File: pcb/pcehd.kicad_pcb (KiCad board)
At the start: 2 copper layers, 158 parts, among them J1 HDMI_CONN, P1 JTAG_CONN, Q1 BC847, Q2 BC847, U1 AP7361, U10 SN74LVCC4245APW, U11 SN74LVCC4245APW, U12 10CL025YE144C8N, U13 IS25LP016D-JBLE, U14 SN74LVCC4245APW, U15 TLV70012, U16 TLV70025, U17 TLV70012, U18 SN74LVCC4245APW, U19 SN74LVC3G17, U2 ADV7513, U3 TLV70018, U4 PCEngineExpansion, U5 FS7140-01G-XTD, U6 PCM1808PWR, U7 SI5351C-B, U8 74153, U9 SN74LVCC4245APW, Y1 25.000MHz

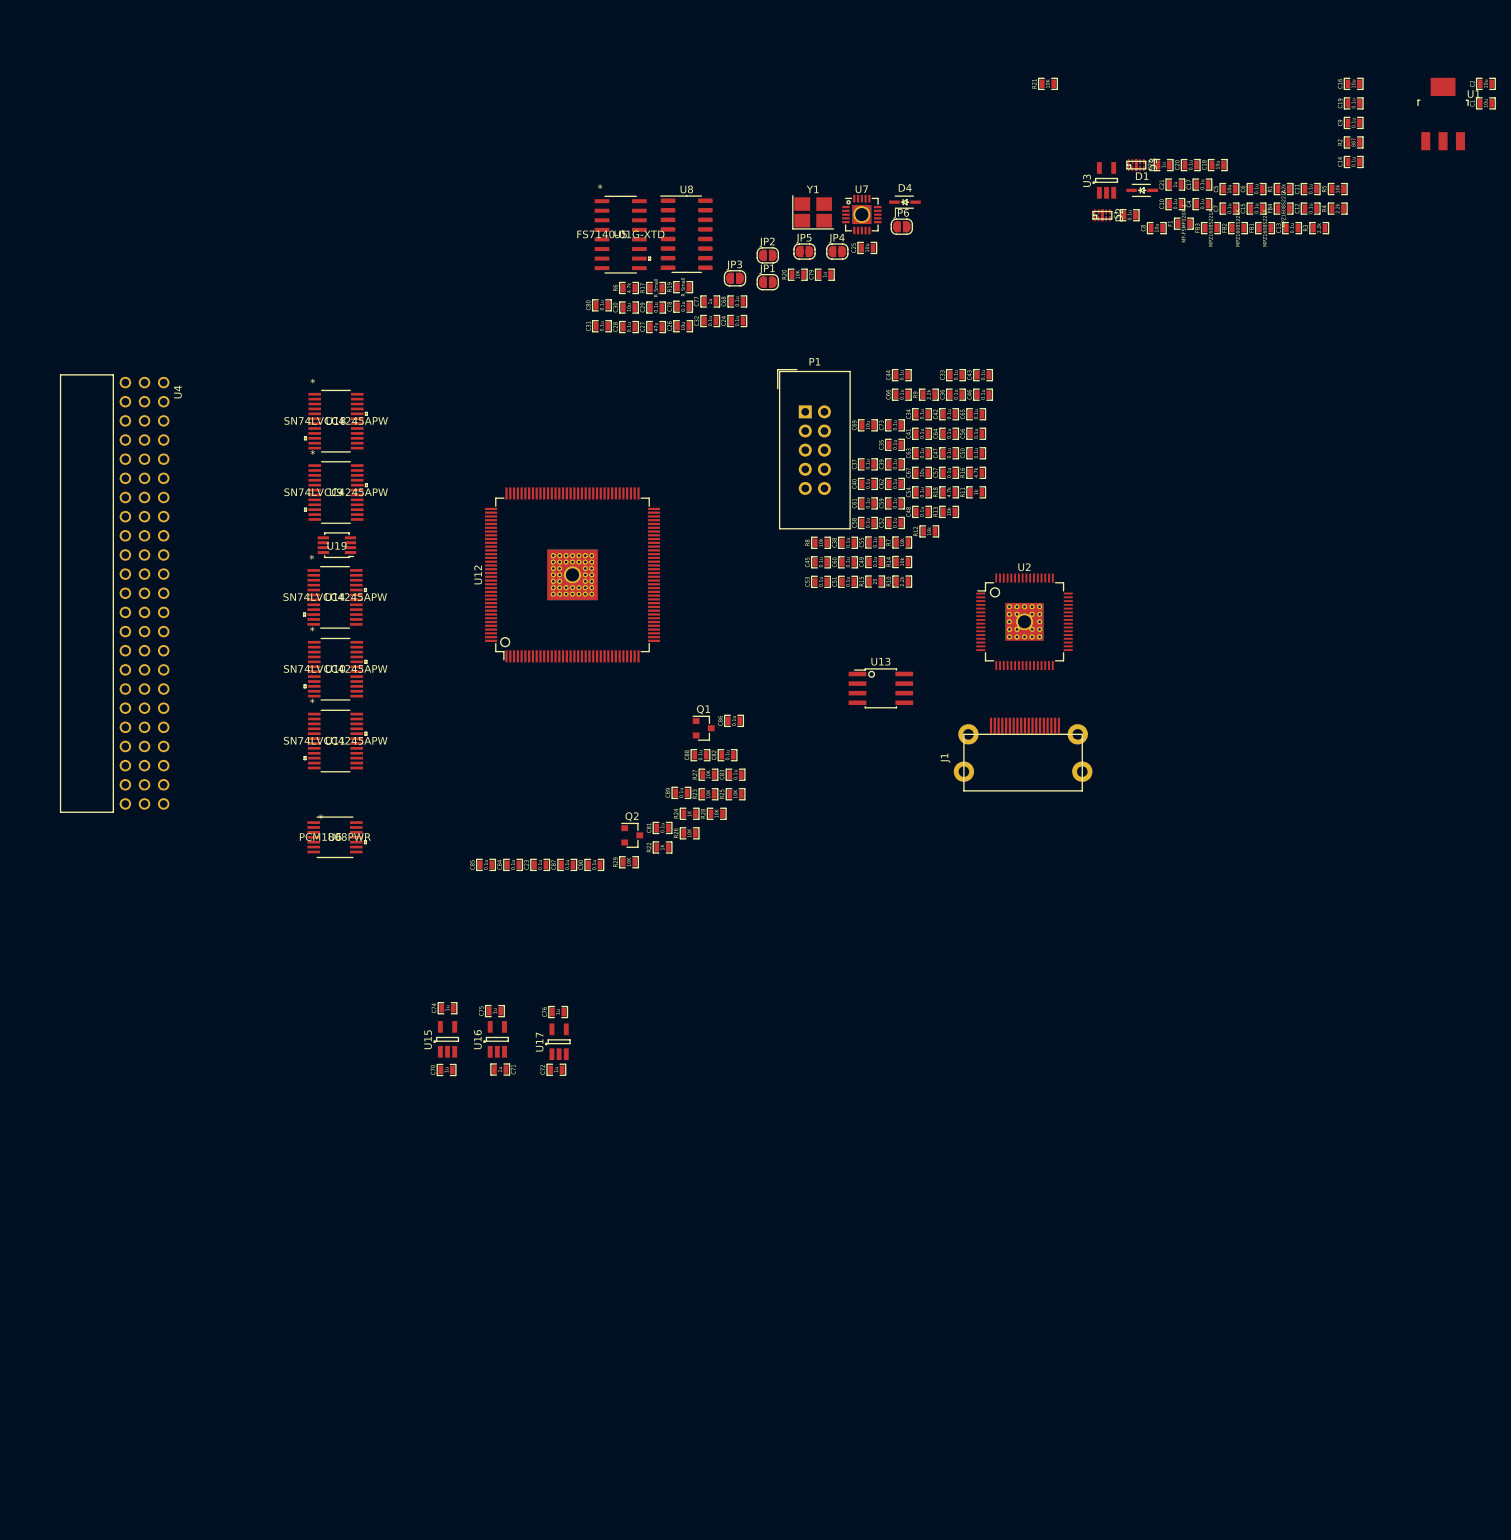
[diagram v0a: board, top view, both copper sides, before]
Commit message: Expansion connection re-order for layout
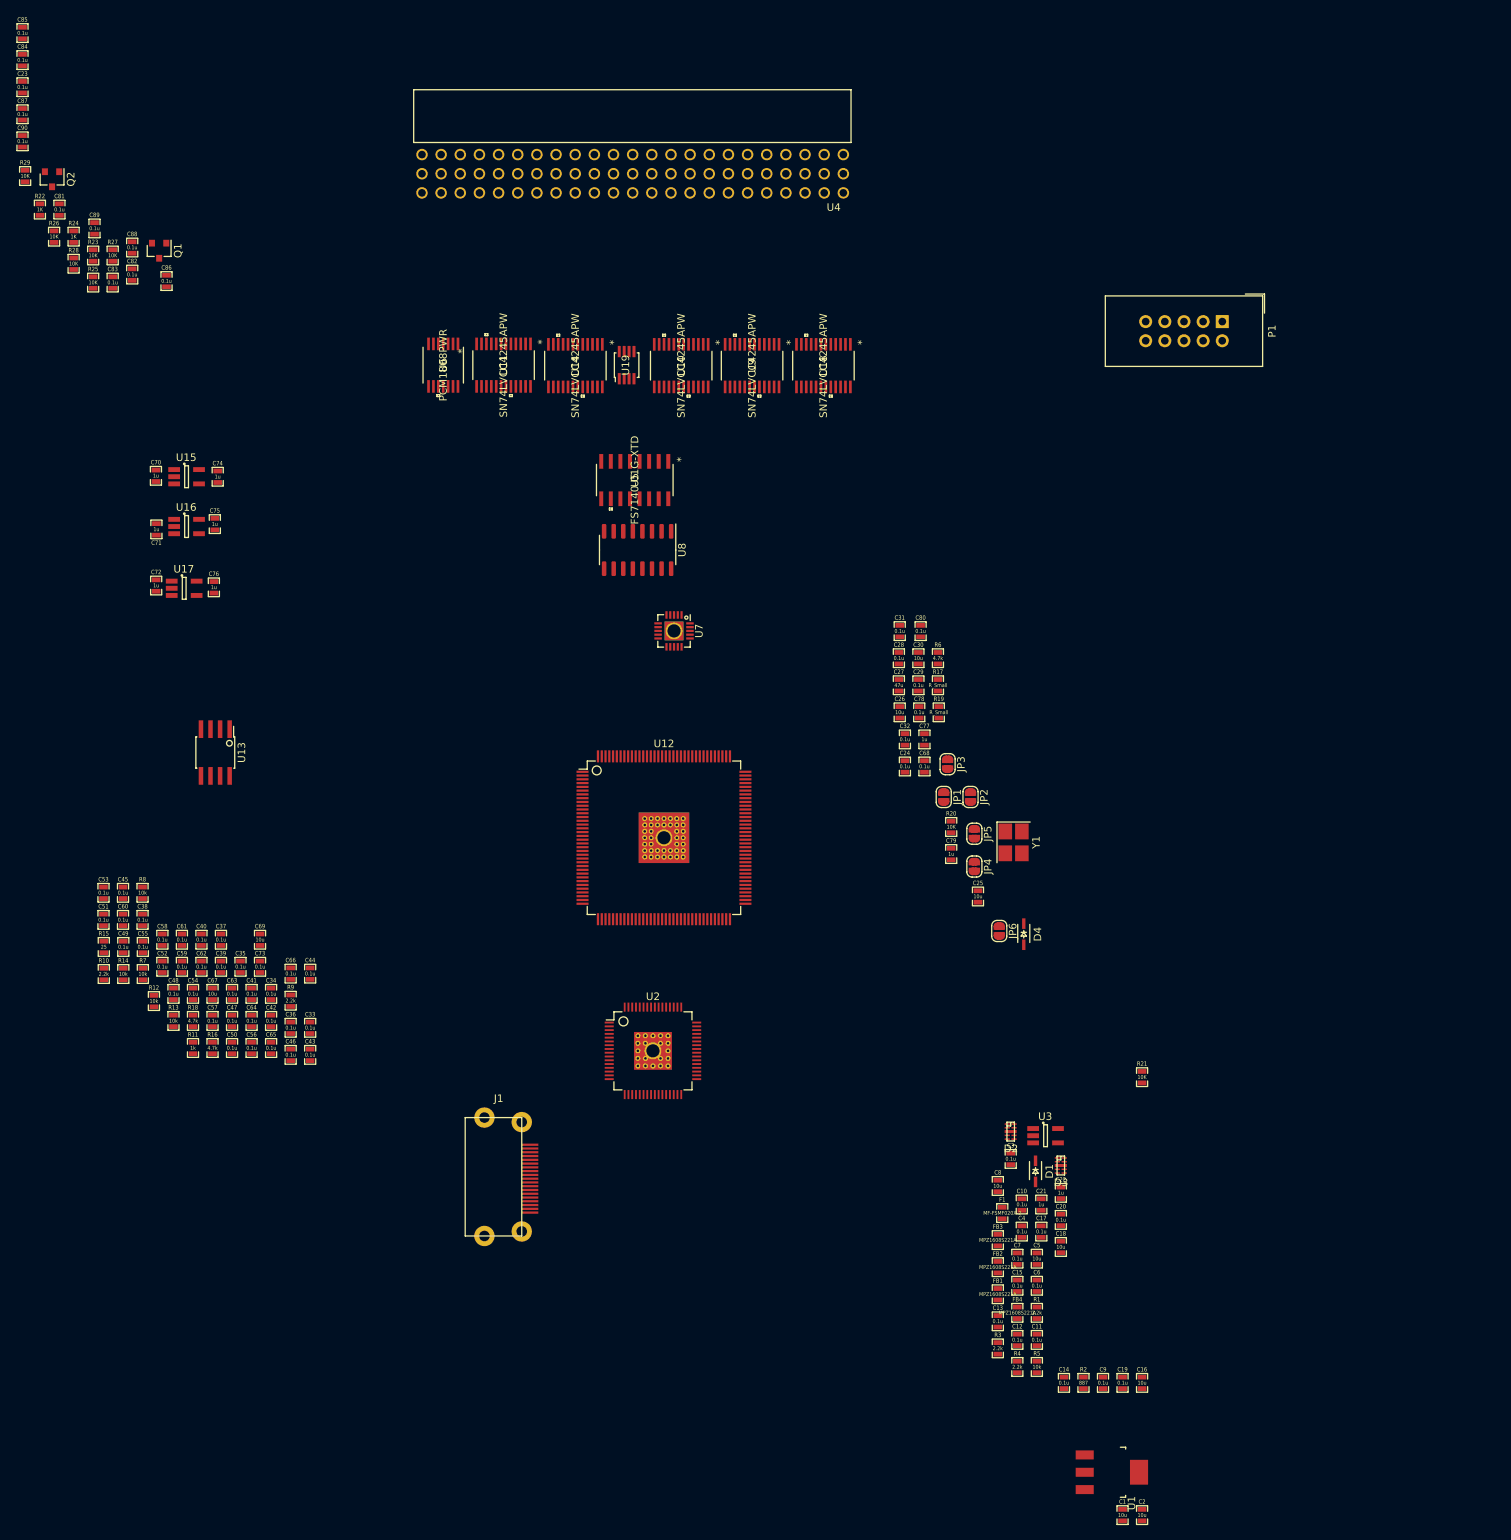
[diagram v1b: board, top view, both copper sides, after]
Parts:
- moved C2 195.2 mm to (175.4, 227.1), turned to 270 degrees
- moved C1 193.3 mm to (172.8, 227.1), turned to 270 degrees
- moved U1 185.4 mm to (171.4, 221.4), turned to 270 degrees
- moved C16 174.5 mm to (175.4, 209.5), turned to 270 degrees
- moved C19 172.4 mm to (172.8, 209.5), turned to 270 degrees
- moved C9 170.4 mm to (170.2, 209.5), turned to 270 degrees
- moved R2 168.4 mm to (167.6, 209.5), turned to 270 degrees
- moved C14 166.4 mm to (165.1, 209.5), turned to 270 degrees
- moved R5 161.2 mm to (161.5, 207.4), turned to 270 degrees
- moved R4 159.4 mm to (158.9, 207.4), turned to 270 degrees
- moved C11 156.9 mm to (161.5, 203.8), turned to 270 degrees
- moved C12 155.0 mm to (158.9, 203.8), turned to 270 degrees
- moved R3 154.6 mm to (156.3, 204.9), turned to 270 degrees
- moved R1 152.6 mm to (161.5, 200.2), turned to 270 degrees
- moved FB4 150.6 mm to (158.9, 200.2), turned to 270 degrees
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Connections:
- U10 pad 14: /fpga1/A15 -> /fpga1/A8
- U10 pad 15: /fpga1/A14 -> /fpga1/A13
- U10 pad 16: /fpga1/A13 -> /fpga1/A10
- U10 pad 17: /fpga1/A12 -> /fpga1/A11
- U10 pad 18: /fpga1/A11 -> /fpga1/A0
- U10 pad 19: /fpga1/A10 -> /fpga1/A2
- U10 pad 20: /fpga1/A9 -> /fpga1/A1
- U10 pad 21: /fpga1/A8 -> /fpga1/A3
- U11 pad 18: /fpga1/A19 -> /fpga1/A18
- U11 pad 19: /fpga1/A18 -> /fpga1/A14
- U11 pad 21: /fpga1/A16 -> /fpga1/A9
- U12 pad 10: /fpga1/A12 -> /fpga1/DDIR
- U12 pad 100: /fpga1/VD5 -> /fpga1/A7
- U12 pad 101: /fpga1/VD6 -> /fpga1/A4
- U12 pad 103: /fpga1/VD7 -> /fpga1/A5
- U12 pad 105: (no net) -> /fpga1/A3
- U12 pad 106: /fpga1/DCKFB -> /fpga1/A1
- U12 pad 11: /fpga1/A13 -> /fpga1/DCKFB
- U12 pad 111: /fpga1/DDIR -> /fpga1/A2
- U12 pad 112: /fpga1/D7 -> /fpga1/A0
- U12 pad 113: /fpga1/D6 -> /fpga1/A11
- U12 pad 114: /fpga1/D5 -> /fpga1/A10
- U12 pad 115: /fpga1/D4 -> /fpga1/A13
- U12 pad 119: /fpga1/D3 -> /fpga1/A8
- U12 pad 120: /fpga1/D2 -> /fpga1/D7
- U12 pad 121: /fpga1/D1 -> /fpga1/D6
- U12 pad 125: /fpga1/D0 -> /fpga1/D5
- U12 pad 126: /fpga1/A0 -> /fpga1/SI_CLK0
- U12 pad 127: /fpga1/A1 -> /fpga1/SI_CLK1
- U12 pad 128: /fpga1/A2 -> /fpga1/DCK
- U12 pad 129: /fpga1/A3 -> /fpga1/CS
- U12 pad 132: /fpga1/A4 -> /fpga1/D4
- U12 pad 133: /fpga1/A5 -> /fpga1/D3
- U12 pad 135: /fpga1/A6 -> /fpga1/D2
- U12 pad 136: /fpga1/A7 -> /fpga1/D1
- U12 pad 137: /fpga1/A8 -> /fpga1/D0
- U12 pad 141: /fpga1/SDA -> /fpga1/A9
- U12 pad 142: /fpga1/SCL -> /fpga1/A17
- U12 pad 143: /fpga1/A9 -> /fpga1/A14
- U12 pad 144: /fpga1/A10 -> /fpga1/A18
- U12 pad 22: /fpga1/SI_CLK0 -> (no net)
- U12 pad 23: /fpga1/SI_CLK1 -> /fpga1/WR_N
- U12 pad 24: /fpga1/DCK -> /fpga1/SPBG
- U12 pad 25: /fpga1/SPBG -> /fpga1/CEK
- U12 pad 28: /fpga1/CS -> /fpga1/CDD
- U12 pad 31: /fpga1/CEK -> /fpga1/RST_N
- U12 pad 32: /fpga1/WR_N -> /fpga1/SDA
- U12 pad 33: (no net) -> /fpga1/SCL
- U12 pad 44: /fpga1/A14 -> /fpga1/B2
- U12 pad 46: /fpga1/CDD -> /fpga1/B3
- U12 pad 49: /fpga1/R4 -> /fpga1/B4
- U12 pad 50: /fpga1/R3 -> /fpga1/B0
- U12 pad 51: /fpga1/R2 -> /fpga1/B1
- U12 pad 52: (no net) -> /fpga1/A19
- U12 pad 54: /fpga1/A16 -> (no net)
- U12 pad 55: /fpga1/A17 -> (no net)
- U12 pad 58: /fpga1/R1 -> /fpga1/G2
- U12 pad 59: /fpga1/R0 -> /fpga1/HDMITX_PCLK
- U12 pad 60: /fpga1/G4 -> /fpga1/G3
- U12 pad 66: /fpga1/G3 -> /fpga1/G4
- U12 pad 67: /fpga1/G2 -> /fpga1/G0
- U12 pad 68: /fpga1/HDMITX_PCLK -> /fpga1/G1
- U12 pad 69: /fpga1/G1 -> /fpga1/R2
- U12 pad 7: /fpga1/A11 -> /fpga1/A20
- U12 pad 71: /fpga1/G0 -> /fpga1/R3
- U12 pad 72: /fpga1/B4 -> /fpga1/R4
- U12 pad 76: /fpga1/B3 -> /fpga1/R0
- U12 pad 77: /fpga1/B2 -> /fpga1/R1
- U12 pad 80: /fpga1/RST_N -> /fpga1/VD0
- U12 pad 83: /fpga1/B1 -> /fpga1/VD1
- U12 pad 85: /fpga1/B0 -> /fpga1/VD2
- U12 pad 86: /fpga1/A18 -> /fpga1/VD3
- U12 pad 87: /fpga1/A19 -> /fpga1/VD4
- U12 pad 88: /fpga1/A20 -> /fpga1/VD5
- U12 pad 89: /fpga1/VD0 -> /fpga1/VD6
- U12 pad 90: /fpga1/VD1 -> /fpga1/VD7
- U12 pad 91: /fpga1/VD2 -> /fpga1/A16
- U12 pad 98: /fpga1/VD3 -> /fpga1/A12
- U12 pad 99: /fpga1/VD4 -> /fpga1/A6
- U14 pad 14: /fpga1/D7 -> /fpga1/D0
- U14 pad 15: /fpga1/D6 -> /fpga1/D1
- U14 pad 16: /fpga1/D5 -> /fpga1/D2
- U14 pad 17: /fpga1/D4 -> /fpga1/D3
- U14 pad 18: /fpga1/D3 -> /fpga1/D4
- U14 pad 19: /fpga1/D2 -> /fpga1/D5
- U14 pad 20: /fpga1/D1 -> /fpga1/D6
- U14 pad 21: /fpga1/D0 -> /fpga1/D7
- U4 pad A4: Net-(U11-Pad5) -> Net-(U11-Pad6)
- U4 pad A5: Net-(U10-Pad9) -> Net-(U11-Pad5)
- U4 pad A6: Net-(U10-Pad4) -> Net-(U11-Pad3)
- U4 pad A7: Net-(U10-Pad5) -> Net-(U10-Pad8)
- U4 pad A8: Net-(U14-Pad4) -> Net-(U14-Pad9)
- U4 pad B10: Net-(U14-Pad8) -> Net-(U14-Pad5)
- U4 pad B12: Net-(U4-PadB12) -> Net-(U10-Pad6)
- U4 pad B13: Net-(U4-PadB13) -> Net-(U10-Pad5)
- U4 pad B17: Net-(U10-Pad7) -> Net-(U4-PadB17)
- U4 pad B18: Net-(U11-Pad3) -> Net-(U4-PadB18)
- U4 pad B6: Net-(U10-Pad3) -> Net-(U10-Pad10)
- U4 pad B8: Net-(U14-Pad3) -> Net-(U14-Pad10)
- U4 pad B9: Net-(U14-Pad6) -> Net-(U14-Pad7)
- U4 pad C10: Net-(U14-Pad7) -> Net-(U14-Pad6)
- U4 pad C11: Net-(U14-Pad9) -> Net-(U14-Pad4)
- U4 pad C12: Net-(U14-Pad10) -> Net-(U14-Pad3)
- U4 pad C13: Net-(U4-PadC13) -> Net-(U10-Pad4)
- U4 pad C14: Net-(U4-PadC14) -> Net-(U10-Pad3)
- U4 pad C18: Net-(U10-Pad10) -> Net-(U4-PadC18)
- U4 pad C19: Net-(U11-Pad6) -> Net-(U4-PadC19)
- U4 pad C6: Net-(U10-Pad8) -> Net-(U10-Pad9)
- U4 pad C7: Net-(U10-Pad6) -> Net-(U10-Pad7)
- U4 pad C9: Net-(U14-Pad5) -> Net-(U14-Pad8)
- U8 pad 3: /fpga1/DCKFB -> Net-(U5-Pad15)
- U8 pad 4: Net-(U5-Pad15) -> Net-(U5-Pad16)
- U8 pad 5: Net-(U5-Pad16) -> /fpga1/DCKFB
- U9 pad 10: Net-(U4-PadB16) -> Net-(U4-PadB15)
- U9 pad 14: /fpga1/A7 -> /fpga1/A5
- U9 pad 15: /fpga1/A6 -> /fpga1/A4
- U9 pad 16: /fpga1/A5 -> /fpga1/A7
- U9 pad 17: /fpga1/A4 -> /fpga1/A6
- U9 pad 18: /fpga1/A3 -> /fpga1/A12
- U9 pad 19: /fpga1/A2 -> /fpga1/A16
- U9 pad 20: /fpga1/A1 -> /fpga1/A15
- U9 pad 21: /fpga1/A0 -> /fpga1/A19
- U9 pad 3: Net-(U4-PadB12) -> Net-(U4-PadC19)
- U9 pad 4: Net-(U4-PadC13) -> Net-(U4-PadC18)
- U9 pad 5: Net-(U4-PadB13) -> Net-(U4-PadB18)
- U9 pad 6: Net-(U4-PadC14) -> Net-(U4-PadB17)
- U9 pad 7: Net-(U4-PadC15) -> Net-(U4-PadC16)
- U9 pad 8: Net-(U4-PadB15) -> Net-(U4-PadB16)
- U9 pad 9: Net-(U4-PadC16) -> Net-(U4-PadC15)
